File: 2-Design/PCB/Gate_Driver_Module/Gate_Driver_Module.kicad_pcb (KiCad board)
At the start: 2 copper layers, 30 x 30 mm, 12 parts, among them J1 Conn_01x04_Male, J2 Conn_01x04_Male, U1 ROE-0512S, U2 LTV-817, U3 TC4421A

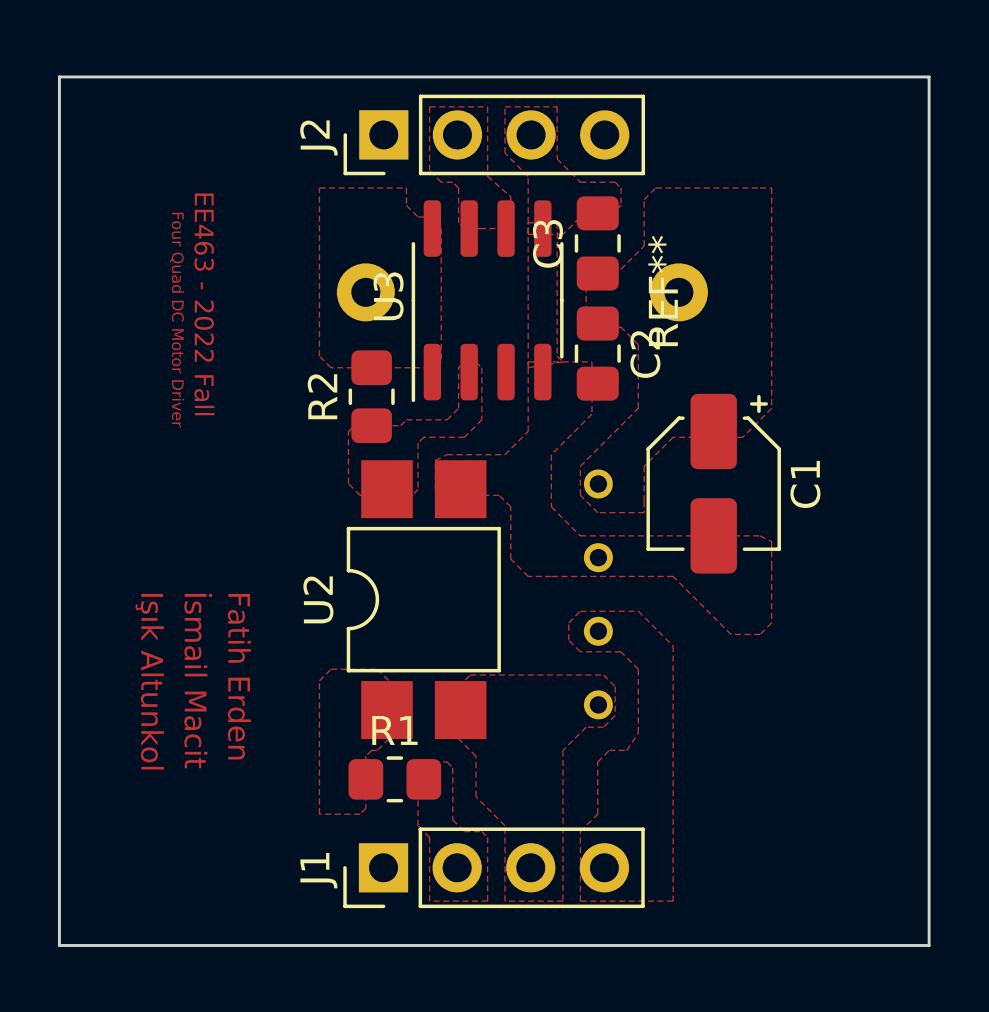
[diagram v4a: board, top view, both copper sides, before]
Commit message: Controller Module v1, tracks to be drawn
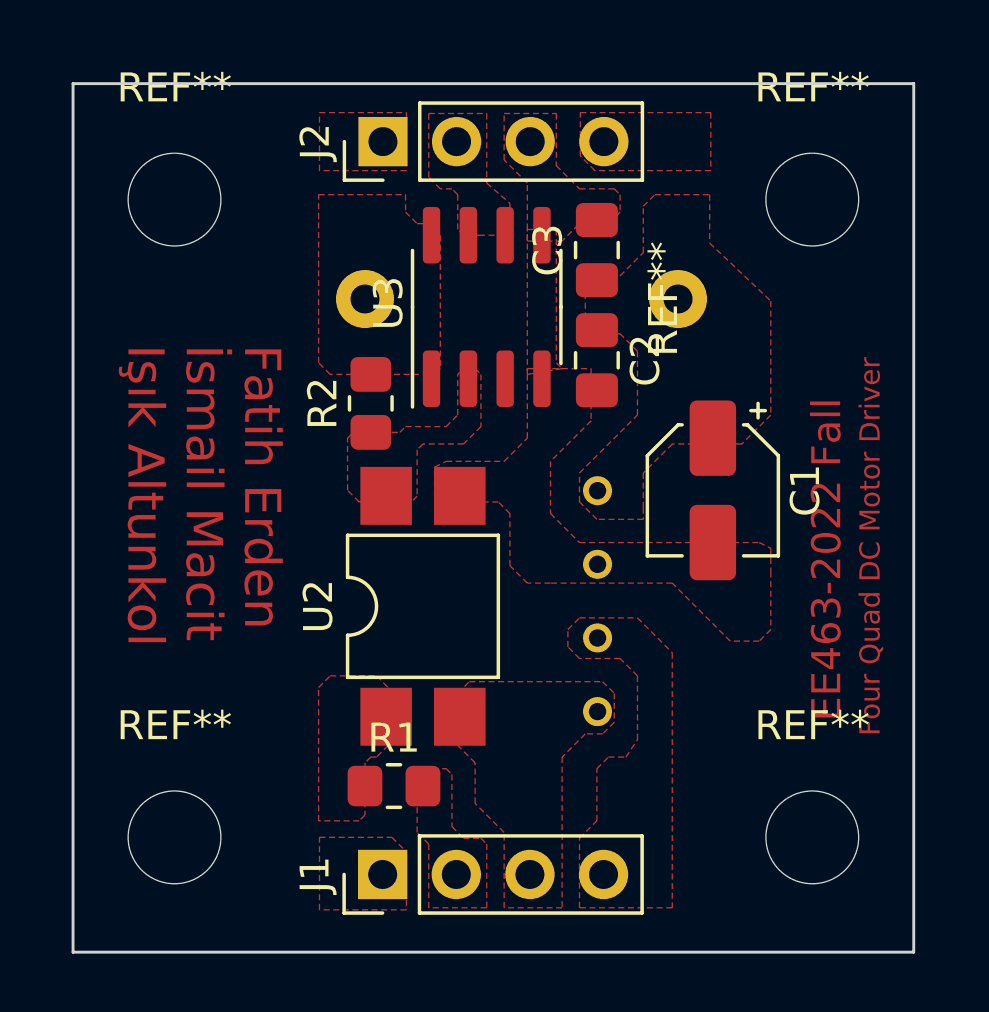
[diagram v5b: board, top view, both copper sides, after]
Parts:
- added REF**: MountingHole_3.2mm_M3_ISO7380, MountingHole:MountingHole_3.2mm_M3_ISO7380, F.Cu at (170.0, 117.0)
- added REF**: MountingHole_3.2mm_M3_ISO7380, MountingHole:MountingHole_3.2mm_M3_ISO7380, F.Cu at (192.0, 117.0)
- added REF**: MountingHole_3.2mm_M3_ISO7380, MountingHole:MountingHole_3.2mm_M3_ISO7380, F.Cu at (192.0, 95.0)
- added REF**: MountingHole_3.2mm_M3_ISO7380, MountingHole:MountingHole_3.2mm_M3_ISO7380, F.Cu at (170.0, 95.0)
- moved ? 0.23 mm to (176.6, 98.4)
- moved C1 0.23 mm to (188.6, 105.0)
- moved C2 0.23 mm to (184.6, 100.5)
- moved C3 0.23 mm to (184.6, 96.7)
- moved J1 0.23 mm to (177.2, 118.3)
- moved J2 0.23 mm to (177.2, 93.0)
- moved R1 0.23 mm to (177.6, 115.2)
- moved R2 0.23 mm to (176.8, 102.0)
- moved REF** 0.23 mm to (187.4, 98.4)
- moved U1 0.23 mm to (184.6, 108.9)
- moved U2 0.23 mm to (178.6, 109.0)
- moved U3 0.23 mm to (180.8, 98.7)
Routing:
- added copper zone on F.Cu, net unconnected-(J1-Pad1)
- added copper zone on F.Cu, net unconnected-(J2-Pad1)
- added copper zone on F.Cu, net unconnected-(J2-Pad4)
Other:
- board size 30 x 30 mm -> 29 x 30 mm
- board text added: "EE463-2022 Fall"
- board text added: "Fatih Erden İsmail Macit Işık Altunkol"
- board text removed: "EE463 - 2022 Fall"
- board text removed: "Fatih Erden"
- board text removed: "Işık Altunkol"
- board text removed: "İsmail Macit"

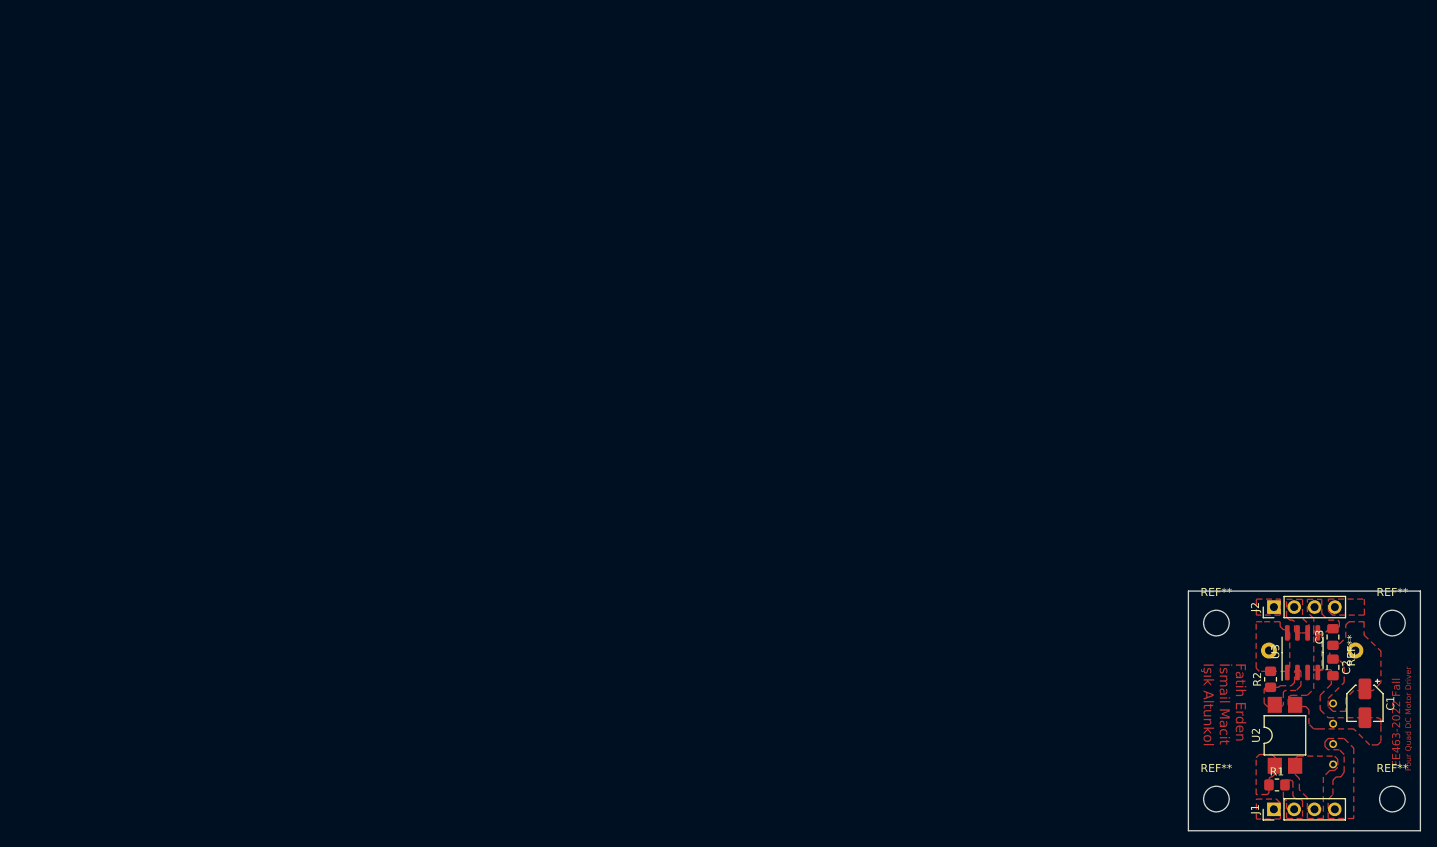
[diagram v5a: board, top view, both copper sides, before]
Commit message: Gate Driver Module minimum load for boost, plus Controller Module advancements
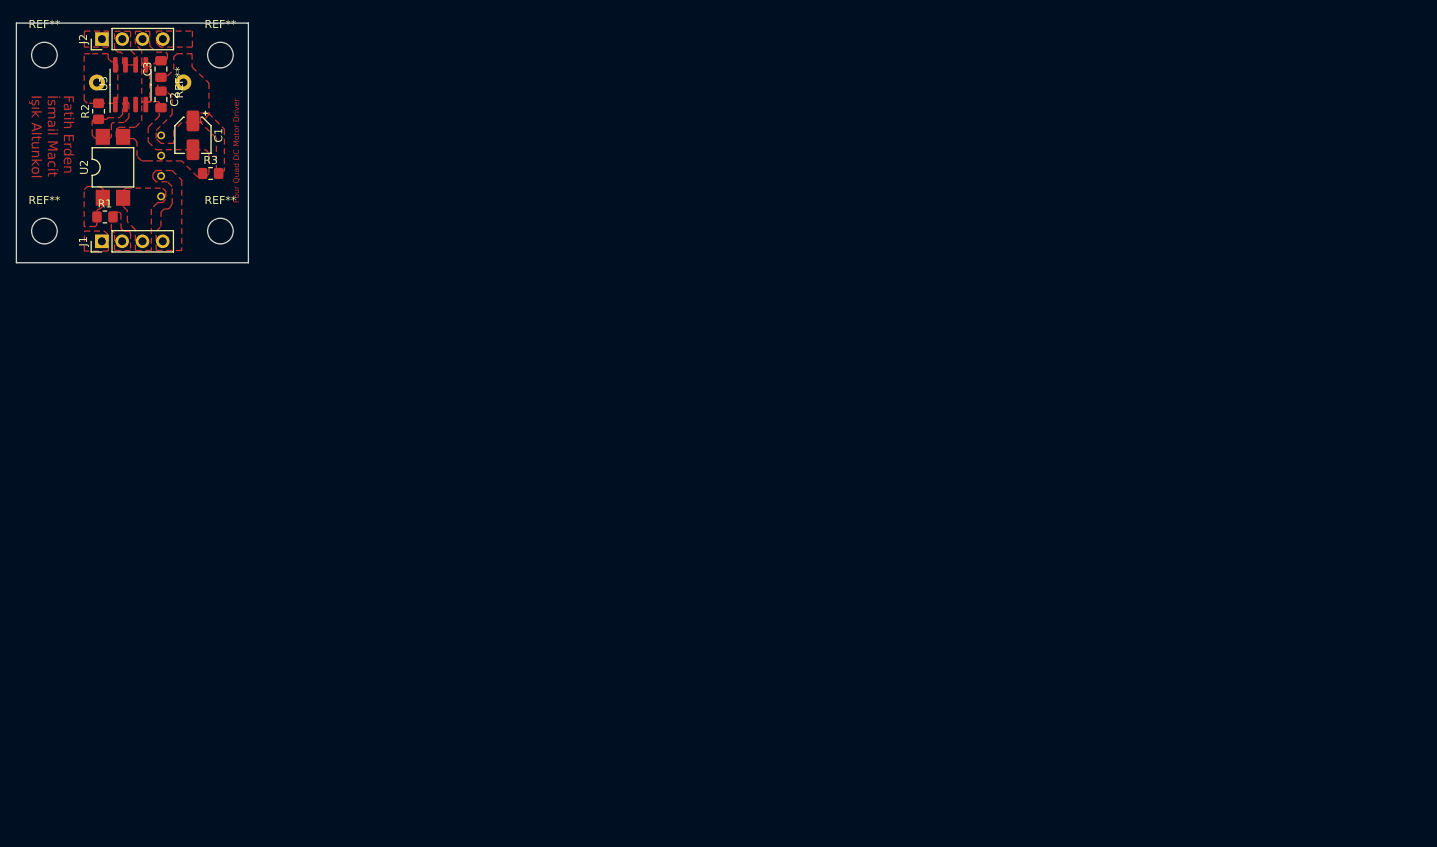
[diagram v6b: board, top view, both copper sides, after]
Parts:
- added R3: 1kR, Resistor_SMD:R_0805_2012Metric_Pad1.20x1.40mm_HandSolder, F.Cu at (44.3, 38.8)
- moved ? 162.8 mm to (30.1, 27.4)
- moved C1 162.8 mm to (42.1, 34.0)
- moved C2 162.8 mm to (38.1, 29.5)
- moved C3 162.8 mm to (38.1, 25.7)
- moved J1 162.8 mm to (30.7, 47.3)
- moved J2 162.8 mm to (30.7, 22.0)
- moved R1 162.8 mm to (31.1, 44.2)
- moved R2 162.8 mm to (30.3, 31.0)
- moved REF** 162.8 mm to (23.5, 46.0)
- moved REF** 162.8 mm to (45.5, 46.0)
- moved REF** 162.8 mm to (45.5, 24.0)
- moved REF** 162.8 mm to (23.5, 24.0)
- moved REF** 162.8 mm to (40.9, 27.4)
- moved U1 162.8 mm to (38.1, 37.9)
- moved U2 162.8 mm to (32.1, 38.0)
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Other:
- board text removed: "EE463-2022 Fall"

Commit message: Some changes i dont even remember
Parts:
- removed the ? at (30.1, 27.4)
- removed the C1 at (42.1, 34.0)
- removed the C2 at (38.1, 29.5)
- removed the C3 at (38.1, 25.7)
- removed the J1 at (30.7, 47.3)
- removed the J2 at (30.7, 22.0)
- removed the R1 at (31.1, 44.2)
- removed the R2 at (30.3, 31.0)
- removed the R3 at (44.3, 38.8)
- removed the REF** at (23.5, 46.0)
- removed the REF** at (45.5, 46.0)
- removed the REF** at (45.5, 24.0)
- removed the REF** at (23.5, 24.0)
- removed the REF** at (40.9, 27.4)
- removed the U1 at (38.1, 37.9)
- removed the U2 at (32.1, 38.0)
- removed the U3 at (34.3, 27.7)
- added ?: , , F.Cu at (71.6, 26.4)
- added ?: , , F.Cu at (246.6, 94.0)
- added ?: , , F.Cu at (211.6, 26.4)
- added ?: , , F.Cu at (176.6, 60.2)
- added ?: , , F.Cu at (141.6, 26.4)
- added ?: , , F.Cu at (106.6, 94.0)
- added ?: , , F.Cu at (176.6, 127.8)
- added ?: , , F.Cu at (211.6, 60.2)
- added ?: , , F.Cu at (246.6, 26.4)
- added ?: , , F.Cu at (176.6, 94.0)
- added ?: , , F.Cu at (211.6, 94.0)
- added ?: , , F.Cu at (176.6, 26.4)
- added ?: , , F.Cu at (141.6, 127.8)
- added ?: , , F.Cu at (106.6, 127.8)
- added ?: , , F.Cu at (71.6, 94.0)
- added ?: , , F.Cu at (106.6, 26.4)
- added ?: , , F.Cu at (141.6, 60.2)
- added ?: , , F.Cu at (106.6, 60.2)
- added ?: , , F.Cu at (141.6, 94.0)
- added ?: , , F.Cu at (71.6, 127.8)
- added ?: , , F.Cu at (246.6, 127.8)
- added ?: , , F.Cu at (71.6, 60.2)
- added ?: , , F.Cu at (246.6, 60.2)
- added ?: , , F.Cu at (211.6, 127.8)
- added C1: 4.7uF, Capacitor_SMD:CP_Elec_4x5.4, F.Cu at (188.6, 134.4)
- added C1: 4.7uF, Capacitor_SMD:CP_Elec_4x5.4, F.Cu at (153.6, 66.8)
- added C1: 4.7uF, Capacitor_SMD:CP_Elec_4x5.4, F.Cu at (83.6, 66.8)
- added C1: 4.7uF, Capacitor_SMD:CP_Elec_4x5.4, F.Cu at (118.6, 100.6)
- added C1: 4.7uF, Capacitor_SMD:CP_Elec_4x5.4, F.Cu at (118.6, 33.0)
- added C1: 4.7uF, Capacitor_SMD:CP_Elec_4x5.4, F.Cu at (188.6, 66.8)
- added C1: 4.7uF, Capacitor_SMD:CP_Elec_4x5.4, F.Cu at (118.6, 66.8)
- added C1: 4.7uF, Capacitor_SMD:CP_Elec_4x5.4, F.Cu at (83.6, 134.4)
- added C1: 4.7uF, Capacitor_SMD:CP_Elec_4x5.4, F.Cu at (153.6, 33.0)
- added C1: 4.7uF, Capacitor_SMD:CP_Elec_4x5.4, F.Cu at (258.6, 66.8)
- added C1: 4.7uF, Capacitor_SMD:CP_Elec_4x5.4, F.Cu at (153.6, 134.4)
- added C1: 4.7uF, Capacitor_SMD:CP_Elec_4x5.4, F.Cu at (153.6, 100.6)
- added C1: 4.7uF, Capacitor_SMD:CP_Elec_4x5.4, F.Cu at (223.6, 100.6)
- added C1: 4.7uF, Capacitor_SMD:CP_Elec_4x5.4, F.Cu at (83.6, 33.0)
- added C1: 4.7uF, Capacitor_SMD:CP_Elec_4x5.4, F.Cu at (258.6, 33.0)
- added C1: 4.7uF, Capacitor_SMD:CP_Elec_4x5.4, F.Cu at (188.6, 33.0)
- added C1: 4.7uF, Capacitor_SMD:CP_Elec_4x5.4, F.Cu at (188.6, 100.6)
- added C1: 4.7uF, Capacitor_SMD:CP_Elec_4x5.4, F.Cu at (223.6, 66.8)
- added C1: 4.7uF, Capacitor_SMD:CP_Elec_4x5.4, F.Cu at (83.6, 100.6)
- added C1: 4.7uF, Capacitor_SMD:CP_Elec_4x5.4, F.Cu at (223.6, 134.4)
- added C1: 4.7uF, Capacitor_SMD:CP_Elec_4x5.4, F.Cu at (258.6, 134.4)
- added C1: 4.7uF, Capacitor_SMD:CP_Elec_4x5.4, F.Cu at (223.6, 33.0)
- added C1: 4.7uF, Capacitor_SMD:CP_Elec_4x5.4, F.Cu at (118.6, 134.4)
- added C1: 4.7uF, Capacitor_SMD:CP_Elec_4x5.4, F.Cu at (258.6, 100.6)
- added C2: 0.1uF, Capacitor_SMD:C_0805_2012Metric_Pad1.18x1.45mm_HandSolder, F.Cu at (149.6, 62.3)
- added C2: 0.1uF, Capacitor_SMD:C_0805_2012Metric_Pad1.18x1.45mm_HandSolder, F.Cu at (114.6, 129.9)
- added C2: 0.1uF, Capacitor_SMD:C_0805_2012Metric_Pad1.18x1.45mm_HandSolder, F.Cu at (219.6, 96.1)
- added C2: 0.1uF, Capacitor_SMD:C_0805_2012Metric_Pad1.18x1.45mm_HandSolder, F.Cu at (149.6, 28.5)
- added C2: 0.1uF, Capacitor_SMD:C_0805_2012Metric_Pad1.18x1.45mm_HandSolder, F.Cu at (79.6, 62.3)
- added C2: 0.1uF, Capacitor_SMD:C_0805_2012Metric_Pad1.18x1.45mm_HandSolder, F.Cu at (79.6, 28.5)
- added C2: 0.1uF, Capacitor_SMD:C_0805_2012Metric_Pad1.18x1.45mm_HandSolder, F.Cu at (254.6, 28.5)
- added C2: 0.1uF, Capacitor_SMD:C_0805_2012Metric_Pad1.18x1.45mm_HandSolder, F.Cu at (184.6, 96.1)
- added C2: 0.1uF, Capacitor_SMD:C_0805_2012Metric_Pad1.18x1.45mm_HandSolder, F.Cu at (184.6, 62.3)
- added C2: 0.1uF, Capacitor_SMD:C_0805_2012Metric_Pad1.18x1.45mm_HandSolder, F.Cu at (184.6, 28.5)
- added C2: 0.1uF, Capacitor_SMD:C_0805_2012Metric_Pad1.18x1.45mm_HandSolder, F.Cu at (114.6, 62.3)
- added C2: 0.1uF, Capacitor_SMD:C_0805_2012Metric_Pad1.18x1.45mm_HandSolder, F.Cu at (114.6, 28.5)
- added C2: 0.1uF, Capacitor_SMD:C_0805_2012Metric_Pad1.18x1.45mm_HandSolder, F.Cu at (79.6, 96.1)
- added C2: 0.1uF, Capacitor_SMD:C_0805_2012Metric_Pad1.18x1.45mm_HandSolder, F.Cu at (149.6, 129.9)
- added C2: 0.1uF, Capacitor_SMD:C_0805_2012Metric_Pad1.18x1.45mm_HandSolder, F.Cu at (219.6, 129.9)
- added C2: 0.1uF, Capacitor_SMD:C_0805_2012Metric_Pad1.18x1.45mm_HandSolder, F.Cu at (184.6, 129.9)
- added C2: 0.1uF, Capacitor_SMD:C_0805_2012Metric_Pad1.18x1.45mm_HandSolder, F.Cu at (219.6, 62.3)
- added C2: 0.1uF, Capacitor_SMD:C_0805_2012Metric_Pad1.18x1.45mm_HandSolder, F.Cu at (219.6, 28.5)
- added C2: 0.1uF, Capacitor_SMD:C_0805_2012Metric_Pad1.18x1.45mm_HandSolder, F.Cu at (254.6, 129.9)
- added C2: 0.1uF, Capacitor_SMD:C_0805_2012Metric_Pad1.18x1.45mm_HandSolder, F.Cu at (114.6, 96.1)
- added C2: 0.1uF, Capacitor_SMD:C_0805_2012Metric_Pad1.18x1.45mm_HandSolder, F.Cu at (254.6, 96.1)
- added C2: 0.1uF, Capacitor_SMD:C_0805_2012Metric_Pad1.18x1.45mm_HandSolder, F.Cu at (79.6, 129.9)
- added C2: 0.1uF, Capacitor_SMD:C_0805_2012Metric_Pad1.18x1.45mm_HandSolder, F.Cu at (254.6, 62.3)
- added C2: 0.1uF, Capacitor_SMD:C_0805_2012Metric_Pad1.18x1.45mm_HandSolder, F.Cu at (149.6, 96.1)
- added C3: 0.1uF, Capacitor_SMD:C_0805_2012Metric_Pad1.18x1.45mm_HandSolder, F.Cu at (114.6, 58.5)
- added C3: 0.1uF, Capacitor_SMD:C_0805_2012Metric_Pad1.18x1.45mm_HandSolder, F.Cu at (184.6, 58.5)
- added C3: 0.1uF, Capacitor_SMD:C_0805_2012Metric_Pad1.18x1.45mm_HandSolder, F.Cu at (79.6, 24.7)
- added C3: 0.1uF, Capacitor_SMD:C_0805_2012Metric_Pad1.18x1.45mm_HandSolder, F.Cu at (114.6, 24.7)
- added C3: 0.1uF, Capacitor_SMD:C_0805_2012Metric_Pad1.18x1.45mm_HandSolder, F.Cu at (219.6, 58.5)
- added C3: 0.1uF, Capacitor_SMD:C_0805_2012Metric_Pad1.18x1.45mm_HandSolder, F.Cu at (219.6, 24.7)
- added C3: 0.1uF, Capacitor_SMD:C_0805_2012Metric_Pad1.18x1.45mm_HandSolder, F.Cu at (149.6, 92.3)
- added C3: 0.1uF, Capacitor_SMD:C_0805_2012Metric_Pad1.18x1.45mm_HandSolder, F.Cu at (79.6, 92.3)
- added C3: 0.1uF, Capacitor_SMD:C_0805_2012Metric_Pad1.18x1.45mm_HandSolder, F.Cu at (219.6, 92.3)
- added C3: 0.1uF, Capacitor_SMD:C_0805_2012Metric_Pad1.18x1.45mm_HandSolder, F.Cu at (184.6, 126.1)
- added C3: 0.1uF, Capacitor_SMD:C_0805_2012Metric_Pad1.18x1.45mm_HandSolder, F.Cu at (184.6, 92.3)
- added C3: 0.1uF, Capacitor_SMD:C_0805_2012Metric_Pad1.18x1.45mm_HandSolder, F.Cu at (149.6, 24.7)
- added C3: 0.1uF, Capacitor_SMD:C_0805_2012Metric_Pad1.18x1.45mm_HandSolder, F.Cu at (254.6, 126.1)
- added C3: 0.1uF, Capacitor_SMD:C_0805_2012Metric_Pad1.18x1.45mm_HandSolder, F.Cu at (149.6, 126.1)
- added C3: 0.1uF, Capacitor_SMD:C_0805_2012Metric_Pad1.18x1.45mm_HandSolder, F.Cu at (254.6, 58.5)
- added C3: 0.1uF, Capacitor_SMD:C_0805_2012Metric_Pad1.18x1.45mm_HandSolder, F.Cu at (254.6, 92.3)
- added C3: 0.1uF, Capacitor_SMD:C_0805_2012Metric_Pad1.18x1.45mm_HandSolder, F.Cu at (184.6, 24.7)
- added C3: 0.1uF, Capacitor_SMD:C_0805_2012Metric_Pad1.18x1.45mm_HandSolder, F.Cu at (149.6, 58.5)
- added C3: 0.1uF, Capacitor_SMD:C_0805_2012Metric_Pad1.18x1.45mm_HandSolder, F.Cu at (79.6, 58.5)
- added C3: 0.1uF, Capacitor_SMD:C_0805_2012Metric_Pad1.18x1.45mm_HandSolder, F.Cu at (114.6, 126.1)
- added C3: 0.1uF, Capacitor_SMD:C_0805_2012Metric_Pad1.18x1.45mm_HandSolder, F.Cu at (254.6, 24.7)
- added C3: 0.1uF, Capacitor_SMD:C_0805_2012Metric_Pad1.18x1.45mm_HandSolder, F.Cu at (114.6, 92.3)
- added C3: 0.1uF, Capacitor_SMD:C_0805_2012Metric_Pad1.18x1.45mm_HandSolder, F.Cu at (79.6, 126.1)
- added C3: 0.1uF, Capacitor_SMD:C_0805_2012Metric_Pad1.18x1.45mm_HandSolder, F.Cu at (219.6, 126.1)
- added J1: Conn_01x04_Male, Connector_PinHeader_2.54mm:PinHeader_1x04_P2.54mm_Vertical, F.Cu at (247.2, 46.3)
- added J1: Conn_01x04_Male, Connector_PinHeader_2.54mm:PinHeader_1x04_P2.54mm_Vertical, F.Cu at (177.2, 80.1)
- added J1: Conn_01x04_Male, Connector_PinHeader_2.54mm:PinHeader_1x04_P2.54mm_Vertical, F.Cu at (247.2, 80.1)
- added J1: Conn_01x04_Male, Connector_PinHeader_2.54mm:PinHeader_1x04_P2.54mm_Vertical, F.Cu at (247.2, 113.9)
- added J1: Conn_01x04_Male, Connector_PinHeader_2.54mm:PinHeader_1x04_P2.54mm_Vertical, F.Cu at (212.2, 113.9)
- added J1: Conn_01x04_Male, Connector_PinHeader_2.54mm:PinHeader_1x04_P2.54mm_Vertical, F.Cu at (72.2, 80.1)
- added J1: Conn_01x04_Male, Connector_PinHeader_2.54mm:PinHeader_1x04_P2.54mm_Vertical, F.Cu at (107.2, 80.1)
- added J1: Conn_01x04_Male, Connector_PinHeader_2.54mm:PinHeader_1x04_P2.54mm_Vertical, F.Cu at (177.2, 113.9)
- added J1: Conn_01x04_Male, Connector_PinHeader_2.54mm:PinHeader_1x04_P2.54mm_Vertical, F.Cu at (107.2, 147.7)
- added J1: Conn_01x04_Male, Connector_PinHeader_2.54mm:PinHeader_1x04_P2.54mm_Vertical, F.Cu at (247.2, 147.7)
- added J1: Conn_01x04_Male, Connector_PinHeader_2.54mm:PinHeader_1x04_P2.54mm_Vertical, F.Cu at (212.2, 147.7)
- added J1: Conn_01x04_Male, Connector_PinHeader_2.54mm:PinHeader_1x04_P2.54mm_Vertical, F.Cu at (212.2, 46.3)
- added J1: Conn_01x04_Male, Connector_PinHeader_2.54mm:PinHeader_1x04_P2.54mm_Vertical, F.Cu at (177.2, 147.7)
- added J1: Conn_01x04_Male, Connector_PinHeader_2.54mm:PinHeader_1x04_P2.54mm_Vertical, F.Cu at (177.2, 46.3)
- added J1: Conn_01x04_Male, Connector_PinHeader_2.54mm:PinHeader_1x04_P2.54mm_Vertical, F.Cu at (72.2, 113.9)
- added J1: Conn_01x04_Male, Connector_PinHeader_2.54mm:PinHeader_1x04_P2.54mm_Vertical, F.Cu at (107.2, 46.3)
- added J1: Conn_01x04_Male, Connector_PinHeader_2.54mm:PinHeader_1x04_P2.54mm_Vertical, F.Cu at (142.2, 113.9)
- added J1: Conn_01x04_Male, Connector_PinHeader_2.54mm:PinHeader_1x04_P2.54mm_Vertical, F.Cu at (212.2, 80.1)
- added J1: Conn_01x04_Male, Connector_PinHeader_2.54mm:PinHeader_1x04_P2.54mm_Vertical, F.Cu at (142.2, 147.7)
- added J1: Conn_01x04_Male, Connector_PinHeader_2.54mm:PinHeader_1x04_P2.54mm_Vertical, F.Cu at (72.2, 147.7)
- added J1: Conn_01x04_Male, Connector_PinHeader_2.54mm:PinHeader_1x04_P2.54mm_Vertical, F.Cu at (142.2, 80.1)
- added J1: Conn_01x04_Male, Connector_PinHeader_2.54mm:PinHeader_1x04_P2.54mm_Vertical, F.Cu at (72.2, 46.3)
- added J1: Conn_01x04_Male, Connector_PinHeader_2.54mm:PinHeader_1x04_P2.54mm_Vertical, F.Cu at (142.2, 46.3)
- added J1: Conn_01x04_Male, Connector_PinHeader_2.54mm:PinHeader_1x04_P2.54mm_Vertical, F.Cu at (107.2, 113.9)
- added J2: Conn_01x04_Male, Connector_PinHeader_2.54mm:PinHeader_1x04_P2.54mm_Vertical, F.Cu at (247.2, 122.4)
- added J2: Conn_01x04_Male, Connector_PinHeader_2.54mm:PinHeader_1x04_P2.54mm_Vertical, F.Cu at (212.2, 21.0)
- added J2: Conn_01x04_Male, Connector_PinHeader_2.54mm:PinHeader_1x04_P2.54mm_Vertical, F.Cu at (107.2, 88.6)
- added J2: Conn_01x04_Male, Connector_PinHeader_2.54mm:PinHeader_1x04_P2.54mm_Vertical, F.Cu at (142.2, 54.8)
- added J2: Conn_01x04_Male, Connector_PinHeader_2.54mm:PinHeader_1x04_P2.54mm_Vertical, F.Cu at (212.2, 122.4)
- added J2: Conn_01x04_Male, Connector_PinHeader_2.54mm:PinHeader_1x04_P2.54mm_Vertical, F.Cu at (177.2, 122.4)
- added J2: Conn_01x04_Male, Connector_PinHeader_2.54mm:PinHeader_1x04_P2.54mm_Vertical, F.Cu at (142.2, 88.6)
- added J2: Conn_01x04_Male, Connector_PinHeader_2.54mm:PinHeader_1x04_P2.54mm_Vertical, F.Cu at (142.2, 122.4)
- added J2: Conn_01x04_Male, Connector_PinHeader_2.54mm:PinHeader_1x04_P2.54mm_Vertical, F.Cu at (212.2, 54.8)
- added J2: Conn_01x04_Male, Connector_PinHeader_2.54mm:PinHeader_1x04_P2.54mm_Vertical, F.Cu at (212.2, 88.6)
- added J2: Conn_01x04_Male, Connector_PinHeader_2.54mm:PinHeader_1x04_P2.54mm_Vertical, F.Cu at (72.2, 88.6)
- added J2: Conn_01x04_Male, Connector_PinHeader_2.54mm:PinHeader_1x04_P2.54mm_Vertical, F.Cu at (247.2, 21.0)
- added J2: Conn_01x04_Male, Connector_PinHeader_2.54mm:PinHeader_1x04_P2.54mm_Vertical, F.Cu at (72.2, 21.0)
- added J2: Conn_01x04_Male, Connector_PinHeader_2.54mm:PinHeader_1x04_P2.54mm_Vertical, F.Cu at (177.2, 88.6)
- added J2: Conn_01x04_Male, Connector_PinHeader_2.54mm:PinHeader_1x04_P2.54mm_Vertical, F.Cu at (72.2, 54.8)
- added J2: Conn_01x04_Male, Connector_PinHeader_2.54mm:PinHeader_1x04_P2.54mm_Vertical, F.Cu at (177.2, 21.0)
- added J2: Conn_01x04_Male, Connector_PinHeader_2.54mm:PinHeader_1x04_P2.54mm_Vertical, F.Cu at (107.2, 21.0)
- added J2: Conn_01x04_Male, Connector_PinHeader_2.54mm:PinHeader_1x04_P2.54mm_Vertical, F.Cu at (72.2, 122.4)
- added J2: Conn_01x04_Male, Connector_PinHeader_2.54mm:PinHeader_1x04_P2.54mm_Vertical, F.Cu at (142.2, 21.0)
- added J2: Conn_01x04_Male, Connector_PinHeader_2.54mm:PinHeader_1x04_P2.54mm_Vertical, F.Cu at (177.2, 54.8)
- added J2: Conn_01x04_Male, Connector_PinHeader_2.54mm:PinHeader_1x04_P2.54mm_Vertical, F.Cu at (107.2, 122.4)
- added J2: Conn_01x04_Male, Connector_PinHeader_2.54mm:PinHeader_1x04_P2.54mm_Vertical, F.Cu at (107.2, 54.8)
- added J2: Conn_01x04_Male, Connector_PinHeader_2.54mm:PinHeader_1x04_P2.54mm_Vertical, F.Cu at (247.2, 88.6)
- added J2: Conn_01x04_Male, Connector_PinHeader_2.54mm:PinHeader_1x04_P2.54mm_Vertical, F.Cu at (247.2, 54.8)
- added R1: 330R, Resistor_SMD:R_0805_2012Metric_Pad1.20x1.40mm_HandSolder, F.Cu at (72.6, 43.2)
- added R1: 330R, Resistor_SMD:R_0805_2012Metric_Pad1.20x1.40mm_HandSolder, F.Cu at (177.6, 43.2)
- added R1: 330R, Resistor_SMD:R_0805_2012Metric_Pad1.20x1.40mm_HandSolder, F.Cu at (212.6, 43.2)
- added R1: 330R, Resistor_SMD:R_0805_2012Metric_Pad1.20x1.40mm_HandSolder, F.Cu at (72.6, 110.8)
- added R1: 330R, Resistor_SMD:R_0805_2012Metric_Pad1.20x1.40mm_HandSolder, F.Cu at (212.6, 110.8)
- added R1: 330R, Resistor_SMD:R_0805_2012Metric_Pad1.20x1.40mm_HandSolder, F.Cu at (247.6, 110.8)
- added R1: 330R, Resistor_SMD:R_0805_2012Metric_Pad1.20x1.40mm_HandSolder, F.Cu at (177.6, 77.0)
- added R1: 330R, Resistor_SMD:R_0805_2012Metric_Pad1.20x1.40mm_HandSolder, F.Cu at (107.6, 77.0)
- added R1: 330R, Resistor_SMD:R_0805_2012Metric_Pad1.20x1.40mm_HandSolder, F.Cu at (142.6, 144.6)
- added R1: 330R, Resistor_SMD:R_0805_2012Metric_Pad1.20x1.40mm_HandSolder, F.Cu at (107.6, 110.8)
- added R1: 330R, Resistor_SMD:R_0805_2012Metric_Pad1.20x1.40mm_HandSolder, F.Cu at (107.6, 144.6)
- added R1: 330R, Resistor_SMD:R_0805_2012Metric_Pad1.20x1.40mm_HandSolder, F.Cu at (212.6, 144.6)
- added R1: 330R, Resistor_SMD:R_0805_2012Metric_Pad1.20x1.40mm_HandSolder, F.Cu at (107.6, 43.2)
- added R1: 330R, Resistor_SMD:R_0805_2012Metric_Pad1.20x1.40mm_HandSolder, F.Cu at (212.6, 77.0)
- added R1: 330R, Resistor_SMD:R_0805_2012Metric_Pad1.20x1.40mm_HandSolder, F.Cu at (177.6, 144.6)
- added R1: 330R, Resistor_SMD:R_0805_2012Metric_Pad1.20x1.40mm_HandSolder, F.Cu at (247.6, 144.6)
- added R1: 330R, Resistor_SMD:R_0805_2012Metric_Pad1.20x1.40mm_HandSolder, F.Cu at (72.6, 77.0)
- added R1: 330R, Resistor_SMD:R_0805_2012Metric_Pad1.20x1.40mm_HandSolder, F.Cu at (247.6, 43.2)
- added R1: 330R, Resistor_SMD:R_0805_2012Metric_Pad1.20x1.40mm_HandSolder, F.Cu at (142.6, 110.8)
- added R1: 330R, Resistor_SMD:R_0805_2012Metric_Pad1.20x1.40mm_HandSolder, F.Cu at (142.6, 43.2)
- added R1: 330R, Resistor_SMD:R_0805_2012Metric_Pad1.20x1.40mm_HandSolder, F.Cu at (247.6, 77.0)
- added R1: 330R, Resistor_SMD:R_0805_2012Metric_Pad1.20x1.40mm_HandSolder, F.Cu at (142.6, 77.0)
- added R1: 330R, Resistor_SMD:R_0805_2012Metric_Pad1.20x1.40mm_HandSolder, F.Cu at (72.6, 144.6)
- added R1: 330R, Resistor_SMD:R_0805_2012Metric_Pad1.20x1.40mm_HandSolder, F.Cu at (177.6, 110.8)
- added R2: 470R, Resistor_SMD:R_0805_2012Metric_Pad1.20x1.40mm_HandSolder, F.Cu at (106.8, 30.0)
- added R2: 470R, Resistor_SMD:R_0805_2012Metric_Pad1.20x1.40mm_HandSolder, F.Cu at (246.8, 97.6)
- added R2: 470R, Resistor_SMD:R_0805_2012Metric_Pad1.20x1.40mm_HandSolder, F.Cu at (141.8, 30.0)
- added R2: 470R, Resistor_SMD:R_0805_2012Metric_Pad1.20x1.40mm_HandSolder, F.Cu at (71.8, 97.6)
- added R2: 470R, Resistor_SMD:R_0805_2012Metric_Pad1.20x1.40mm_HandSolder, F.Cu at (246.8, 131.4)
- added R2: 470R, Resistor_SMD:R_0805_2012Metric_Pad1.20x1.40mm_HandSolder, F.Cu at (176.8, 63.8)
- added R2: 470R, Resistor_SMD:R_0805_2012Metric_Pad1.20x1.40mm_HandSolder, F.Cu at (71.8, 131.4)
- added R2: 470R, Resistor_SMD:R_0805_2012Metric_Pad1.20x1.40mm_HandSolder, F.Cu at (211.8, 63.8)
- added R2: 470R, Resistor_SMD:R_0805_2012Metric_Pad1.20x1.40mm_HandSolder, F.Cu at (176.8, 131.4)
- added R2: 470R, Resistor_SMD:R_0805_2012Metric_Pad1.20x1.40mm_HandSolder, F.Cu at (106.8, 97.6)
- added R2: 470R, Resistor_SMD:R_0805_2012Metric_Pad1.20x1.40mm_HandSolder, F.Cu at (141.8, 63.8)
- added R2: 470R, Resistor_SMD:R_0805_2012Metric_Pad1.20x1.40mm_HandSolder, F.Cu at (246.8, 30.0)
- added R2: 470R, Resistor_SMD:R_0805_2012Metric_Pad1.20x1.40mm_HandSolder, F.Cu at (211.8, 97.6)
- added R2: 470R, Resistor_SMD:R_0805_2012Metric_Pad1.20x1.40mm_HandSolder, F.Cu at (141.8, 97.6)
- added R2: 470R, Resistor_SMD:R_0805_2012Metric_Pad1.20x1.40mm_HandSolder, F.Cu at (71.8, 63.8)
- added R2: 470R, Resistor_SMD:R_0805_2012Metric_Pad1.20x1.40mm_HandSolder, F.Cu at (141.8, 131.4)
- added R2: 470R, Resistor_SMD:R_0805_2012Metric_Pad1.20x1.40mm_HandSolder, F.Cu at (176.8, 97.6)
- added R2: 470R, Resistor_SMD:R_0805_2012Metric_Pad1.20x1.40mm_HandSolder, F.Cu at (211.8, 131.4)
- added R2: 470R, Resistor_SMD:R_0805_2012Metric_Pad1.20x1.40mm_HandSolder, F.Cu at (176.8, 30.0)
- added R2: 470R, Resistor_SMD:R_0805_2012Metric_Pad1.20x1.40mm_HandSolder, F.Cu at (211.8, 30.0)
- added R2: 470R, Resistor_SMD:R_0805_2012Metric_Pad1.20x1.40mm_HandSolder, F.Cu at (106.8, 131.4)
- added R2: 470R, Resistor_SMD:R_0805_2012Metric_Pad1.20x1.40mm_HandSolder, F.Cu at (71.8, 30.0)
- added R2: 470R, Resistor_SMD:R_0805_2012Metric_Pad1.20x1.40mm_HandSolder, F.Cu at (246.8, 63.8)
- added R2: 470R, Resistor_SMD:R_0805_2012Metric_Pad1.20x1.40mm_HandSolder, F.Cu at (106.8, 63.8)
- added R3: 1kR, Resistor_SMD:R_0805_2012Metric_Pad1.20x1.40mm_HandSolder, F.Cu at (85.8, 105.4)
- added R3: 1kR, Resistor_SMD:R_0805_2012Metric_Pad1.20x1.40mm_HandSolder, F.Cu at (225.8, 105.4)
- added R3: 1kR, Resistor_SMD:R_0805_2012Metric_Pad1.20x1.40mm_HandSolder, F.Cu at (155.8, 105.4)
- added R3: 1kR, Resistor_SMD:R_0805_2012Metric_Pad1.20x1.40mm_HandSolder, F.Cu at (260.8, 37.8)
- added R3: 1kR, Resistor_SMD:R_0805_2012Metric_Pad1.20x1.40mm_HandSolder, F.Cu at (85.8, 37.8)
- added R3: 1kR, Resistor_SMD:R_0805_2012Metric_Pad1.20x1.40mm_HandSolder, F.Cu at (190.8, 37.8)
- added R3: 1kR, Resistor_SMD:R_0805_2012Metric_Pad1.20x1.40mm_HandSolder, F.Cu at (190.8, 71.6)
- added R3: 1kR, Resistor_SMD:R_0805_2012Metric_Pad1.20x1.40mm_HandSolder, F.Cu at (190.8, 105.4)
- added R3: 1kR, Resistor_SMD:R_0805_2012Metric_Pad1.20x1.40mm_HandSolder, F.Cu at (190.8, 139.2)
- added R3: 1kR, Resistor_SMD:R_0805_2012Metric_Pad1.20x1.40mm_HandSolder, F.Cu at (225.8, 71.6)
- added R3: 1kR, Resistor_SMD:R_0805_2012Metric_Pad1.20x1.40mm_HandSolder, F.Cu at (85.8, 139.2)
- added R3: 1kR, Resistor_SMD:R_0805_2012Metric_Pad1.20x1.40mm_HandSolder, F.Cu at (155.8, 37.8)
- added R3: 1kR, Resistor_SMD:R_0805_2012Metric_Pad1.20x1.40mm_HandSolder, F.Cu at (260.8, 105.4)
- added R3: 1kR, Resistor_SMD:R_0805_2012Metric_Pad1.20x1.40mm_HandSolder, F.Cu at (120.8, 71.6)
- added R3: 1kR, Resistor_SMD:R_0805_2012Metric_Pad1.20x1.40mm_HandSolder, F.Cu at (120.8, 37.8)
- added R3: 1kR, Resistor_SMD:R_0805_2012Metric_Pad1.20x1.40mm_HandSolder, F.Cu at (260.8, 71.6)
- added R3: 1kR, Resistor_SMD:R_0805_2012Metric_Pad1.20x1.40mm_HandSolder, F.Cu at (225.8, 139.2)
- added R3: 1kR, Resistor_SMD:R_0805_2012Metric_Pad1.20x1.40mm_HandSolder, F.Cu at (85.8, 71.6)
- added R3: 1kR, Resistor_SMD:R_0805_2012Metric_Pad1.20x1.40mm_HandSolder, F.Cu at (120.8, 139.2)
- added R3: 1kR, Resistor_SMD:R_0805_2012Metric_Pad1.20x1.40mm_HandSolder, F.Cu at (225.8, 37.8)
- added R3: 1kR, Resistor_SMD:R_0805_2012Metric_Pad1.20x1.40mm_HandSolder, F.Cu at (155.8, 139.2)
- added R3: 1kR, Resistor_SMD:R_0805_2012Metric_Pad1.20x1.40mm_HandSolder, F.Cu at (260.8, 139.2)
- added R3: 1kR, Resistor_SMD:R_0805_2012Metric_Pad1.20x1.40mm_HandSolder, F.Cu at (155.8, 71.6)
- added R3: 1kR, Resistor_SMD:R_0805_2012Metric_Pad1.20x1.40mm_HandSolder, F.Cu at (120.8, 105.4)
- added REF**: Jumper_Wire_Hole, ee463_footprint_lib:Jumper_Wire_Hole, F.Cu at (187.4, 60.2)
- added REF**: MountingHole_3.2mm_M3_ISO7380, MountingHole:MountingHole_3.2mm_M3_ISO7380, F.Cu at (122.0, 124.4)
- added REF**: Jumper_Wire_Hole, ee463_footprint_lib:Jumper_Wire_Hole, F.Cu at (257.4, 60.2)
- added REF**: MountingHole_3.2mm_M3_ISO7380, MountingHole:MountingHole_3.2mm_M3_ISO7380, F.Cu at (135.0, 112.6)
- added REF**: MountingHole_3.2mm_M3_ISO7380, MountingHole:MountingHole_3.2mm_M3_ISO7380, F.Cu at (192.0, 112.6)
- added REF**: MountingHole_3.2mm_M3_ISO7380, MountingHole:MountingHole_3.2mm_M3_ISO7380, F.Cu at (170.0, 124.4)
- added REF**: MountingHole_3.2mm_M3_ISO7380, MountingHole:MountingHole_3.2mm_M3_ISO7380, F.Cu at (240.0, 124.4)
- added REF**: MountingHole_3.2mm_M3_ISO7380, MountingHole:MountingHole_3.2mm_M3_ISO7380, F.Cu at (100.0, 78.8)
- added REF**: MountingHole_3.2mm_M3_ISO7380, MountingHole:MountingHole_3.2mm_M3_ISO7380, F.Cu at (205.0, 124.4)
- added REF**: MountingHole_3.2mm_M3_ISO7380, MountingHole:MountingHole_3.2mm_M3_ISO7380, F.Cu at (192.0, 56.8)
- added REF**: MountingHole_3.2mm_M3_ISO7380, MountingHole:MountingHole_3.2mm_M3_ISO7380, F.Cu at (205.0, 45.0)
- added REF**: MountingHole_3.2mm_M3_ISO7380, MountingHole:MountingHole_3.2mm_M3_ISO7380, F.Cu at (157.0, 23.0)
- added REF**: MountingHole_3.2mm_M3_ISO7380, MountingHole:MountingHole_3.2mm_M3_ISO7380, F.Cu at (170.0, 90.6)
- added REF**: Jumper_Wire_Hole, ee463_footprint_lib:Jumper_Wire_Hole, F.Cu at (117.4, 60.2)
- added REF**: MountingHole_3.2mm_M3_ISO7380, MountingHole:MountingHole_3.2mm_M3_ISO7380, F.Cu at (240.0, 146.4)
- added REF**: Jumper_Wire_Hole, ee463_footprint_lib:Jumper_Wire_Hole, F.Cu at (222.4, 94.0)
- added REF**: Jumper_Wire_Hole, ee463_footprint_lib:Jumper_Wire_Hole, F.Cu at (117.4, 127.8)
- added REF**: MountingHole_3.2mm_M3_ISO7380, MountingHole:MountingHole_3.2mm_M3_ISO7380, F.Cu at (157.0, 45.0)
- added REF**: MountingHole_3.2mm_M3_ISO7380, MountingHole:MountingHole_3.2mm_M3_ISO7380, F.Cu at (87.0, 124.4)
- added REF**: MountingHole_3.2mm_M3_ISO7380, MountingHole:MountingHole_3.2mm_M3_ISO7380, F.Cu at (65.0, 90.6)
- added REF**: MountingHole_3.2mm_M3_ISO7380, MountingHole:MountingHole_3.2mm_M3_ISO7380, F.Cu at (170.0, 112.6)
- added REF**: MountingHole_3.2mm_M3_ISO7380, MountingHole:MountingHole_3.2mm_M3_ISO7380, F.Cu at (240.0, 23.0)
- added REF**: MountingHole_3.2mm_M3_ISO7380, MountingHole:MountingHole_3.2mm_M3_ISO7380, F.Cu at (135.0, 124.4)
- added REF**: MountingHole_3.2mm_M3_ISO7380, MountingHole:MountingHole_3.2mm_M3_ISO7380, F.Cu at (192.0, 146.4)
- added REF**: MountingHole_3.2mm_M3_ISO7380, MountingHole:MountingHole_3.2mm_M3_ISO7380, F.Cu at (170.0, 56.8)
- added REF**: MountingHole_3.2mm_M3_ISO7380, MountingHole:MountingHole_3.2mm_M3_ISO7380, F.Cu at (262.0, 56.8)
- added REF**: MountingHole_3.2mm_M3_ISO7380, MountingHole:MountingHole_3.2mm_M3_ISO7380, F.Cu at (262.0, 45.0)
- added REF**: MountingHole_3.2mm_M3_ISO7380, MountingHole:MountingHole_3.2mm_M3_ISO7380, F.Cu at (157.0, 146.4)
- added REF**: MountingHole_3.2mm_M3_ISO7380, MountingHole:MountingHole_3.2mm_M3_ISO7380, F.Cu at (135.0, 45.0)
- added REF**: MountingHole_3.2mm_M3_ISO7380, MountingHole:MountingHole_3.2mm_M3_ISO7380, F.Cu at (135.0, 56.8)
- added REF**: MountingHole_3.2mm_M3_ISO7380, MountingHole:MountingHole_3.2mm_M3_ISO7380, F.Cu at (240.0, 56.8)
- added REF**: MountingHole_3.2mm_M3_ISO7380, MountingHole:MountingHole_3.2mm_M3_ISO7380, F.Cu at (122.0, 112.6)
- added REF**: MountingHole_3.2mm_M3_ISO7380, MountingHole:MountingHole_3.2mm_M3_ISO7380, F.Cu at (192.0, 45.0)
- added REF**: MountingHole_3.2mm_M3_ISO7380, MountingHole:MountingHole_3.2mm_M3_ISO7380, F.Cu at (205.0, 112.6)
- added REF**: MountingHole_3.2mm_M3_ISO7380, MountingHole:MountingHole_3.2mm_M3_ISO7380, F.Cu at (87.0, 90.6)
- added REF**: MountingHole_3.2mm_M3_ISO7380, MountingHole:MountingHole_3.2mm_M3_ISO7380, F.Cu at (65.0, 56.8)
- added REF**: MountingHole_3.2mm_M3_ISO7380, MountingHole:MountingHole_3.2mm_M3_ISO7380, F.Cu at (87.0, 45.0)
- added REF**: Jumper_Wire_Hole, ee463_footprint_lib:Jumper_Wire_Hole, F.Cu at (187.4, 94.0)
- added REF**: MountingHole_3.2mm_M3_ISO7380, MountingHole:MountingHole_3.2mm_M3_ISO7380, F.Cu at (227.0, 112.6)
- added REF**: MountingHole_3.2mm_M3_ISO7380, MountingHole:MountingHole_3.2mm_M3_ISO7380, F.Cu at (192.0, 78.8)
- added REF**: MountingHole_3.2mm_M3_ISO7380, MountingHole:MountingHole_3.2mm_M3_ISO7380, F.Cu at (192.0, 23.0)
- added REF**: MountingHole_3.2mm_M3_ISO7380, MountingHole:MountingHole_3.2mm_M3_ISO7380, F.Cu at (157.0, 124.4)
- added REF**: MountingHole_3.2mm_M3_ISO7380, MountingHole:MountingHole_3.2mm_M3_ISO7380, F.Cu at (135.0, 78.8)
- added REF**: Jumper_Wire_Hole, ee463_footprint_lib:Jumper_Wire_Hole, F.Cu at (257.4, 26.4)
- added REF**: MountingHole_3.2mm_M3_ISO7380, MountingHole:MountingHole_3.2mm_M3_ISO7380, F.Cu at (240.0, 112.6)
- added REF**: MountingHole_3.2mm_M3_ISO7380, MountingHole:MountingHole_3.2mm_M3_ISO7380, F.Cu at (100.0, 45.0)
- added REF**: MountingHole_3.2mm_M3_ISO7380, MountingHole:MountingHole_3.2mm_M3_ISO7380, F.Cu at (240.0, 45.0)
- added REF**: MountingHole_3.2mm_M3_ISO7380, MountingHole:MountingHole_3.2mm_M3_ISO7380, F.Cu at (170.0, 78.8)
- added REF**: MountingHole_3.2mm_M3_ISO7380, MountingHole:MountingHole_3.2mm_M3_ISO7380, F.Cu at (100.0, 112.6)
- added REF**: MountingHole_3.2mm_M3_ISO7380, MountingHole:MountingHole_3.2mm_M3_ISO7380, F.Cu at (192.0, 124.4)
- added REF**: MountingHole_3.2mm_M3_ISO7380, MountingHole:MountingHole_3.2mm_M3_ISO7380, F.Cu at (205.0, 90.6)
- added REF**: Jumper_Wire_Hole, ee463_footprint_lib:Jumper_Wire_Hole, F.Cu at (257.4, 94.0)
- added REF**: MountingHole_3.2mm_M3_ISO7380, MountingHole:MountingHole_3.2mm_M3_ISO7380, F.Cu at (227.0, 56.8)
- added REF**: Jumper_Wire_Hole, ee463_footprint_lib:Jumper_Wire_Hole, F.Cu at (222.4, 26.4)
- added REF**: MountingHole_3.2mm_M3_ISO7380, MountingHole:MountingHole_3.2mm_M3_ISO7380, F.Cu at (65.0, 146.4)
- added REF**: Jumper_Wire_Hole, ee463_footprint_lib:Jumper_Wire_Hole, F.Cu at (82.4, 60.2)
- added REF**: MountingHole_3.2mm_M3_ISO7380, MountingHole:MountingHole_3.2mm_M3_ISO7380, F.Cu at (87.0, 56.8)
- added REF**: MountingHole_3.2mm_M3_ISO7380, MountingHole:MountingHole_3.2mm_M3_ISO7380, F.Cu at (122.0, 78.8)
- added REF**: MountingHole_3.2mm_M3_ISO7380, MountingHole:MountingHole_3.2mm_M3_ISO7380, F.Cu at (262.0, 23.0)
- added REF**: MountingHole_3.2mm_M3_ISO7380, MountingHole:MountingHole_3.2mm_M3_ISO7380, F.Cu at (262.0, 90.6)
- added REF**: MountingHole_3.2mm_M3_ISO7380, MountingHole:MountingHole_3.2mm_M3_ISO7380, F.Cu at (65.0, 112.6)
- added REF**: MountingHole_3.2mm_M3_ISO7380, MountingHole:MountingHole_3.2mm_M3_ISO7380, F.Cu at (157.0, 90.6)
- added REF**: MountingHole_3.2mm_M3_ISO7380, MountingHole:MountingHole_3.2mm_M3_ISO7380, F.Cu at (65.0, 78.8)
- added REF**: MountingHole_3.2mm_M3_ISO7380, MountingHole:MountingHole_3.2mm_M3_ISO7380, F.Cu at (262.0, 78.8)
- added REF**: Jumper_Wire_Hole, ee463_footprint_lib:Jumper_Wire_Hole, F.Cu at (187.4, 26.4)
- added REF**: MountingHole_3.2mm_M3_ISO7380, MountingHole:MountingHole_3.2mm_M3_ISO7380, F.Cu at (157.0, 78.8)
- added REF**: MountingHole_3.2mm_M3_ISO7380, MountingHole:MountingHole_3.2mm_M3_ISO7380, F.Cu at (262.0, 112.6)
- added REF**: Jumper_Wire_Hole, ee463_footprint_lib:Jumper_Wire_Hole, F.Cu at (257.4, 127.8)
- added REF**: Jumper_Wire_Hole, ee463_footprint_lib:Jumper_Wire_Hole, F.Cu at (187.4, 127.8)
- added REF**: MountingHole_3.2mm_M3_ISO7380, MountingHole:MountingHole_3.2mm_M3_ISO7380, F.Cu at (65.0, 45.0)
- added REF**: MountingHole_3.2mm_M3_ISO7380, MountingHole:MountingHole_3.2mm_M3_ISO7380, F.Cu at (192.0, 90.6)
- added REF**: MountingHole_3.2mm_M3_ISO7380, MountingHole:MountingHole_3.2mm_M3_ISO7380, F.Cu at (205.0, 78.8)
- added REF**: MountingHole_3.2mm_M3_ISO7380, MountingHole:MountingHole_3.2mm_M3_ISO7380, F.Cu at (65.0, 124.4)
- added REF**: MountingHole_3.2mm_M3_ISO7380, MountingHole:MountingHole_3.2mm_M3_ISO7380, F.Cu at (100.0, 146.4)
- added REF**: MountingHole_3.2mm_M3_ISO7380, MountingHole:MountingHole_3.2mm_M3_ISO7380, F.Cu at (157.0, 56.8)
- added REF**: Jumper_Wire_Hole, ee463_footprint_lib:Jumper_Wire_Hole, F.Cu at (222.4, 60.2)
- added REF**: Jumper_Wire_Hole, ee463_footprint_lib:Jumper_Wire_Hole, F.Cu at (152.4, 127.8)
- added REF**: MountingHole_3.2mm_M3_ISO7380, MountingHole:MountingHole_3.2mm_M3_ISO7380, F.Cu at (170.0, 146.4)
- added REF**: MountingHole_3.2mm_M3_ISO7380, MountingHole:MountingHole_3.2mm_M3_ISO7380, F.Cu at (122.0, 90.6)
- added REF**: MountingHole_3.2mm_M3_ISO7380, MountingHole:MountingHole_3.2mm_M3_ISO7380, F.Cu at (87.0, 78.8)
- added REF**: MountingHole_3.2mm_M3_ISO7380, MountingHole:MountingHole_3.2mm_M3_ISO7380, F.Cu at (100.0, 90.6)
- added REF**: Jumper_Wire_Hole, ee463_footprint_lib:Jumper_Wire_Hole, F.Cu at (222.4, 127.8)
- added REF**: MountingHole_3.2mm_M3_ISO7380, MountingHole:MountingHole_3.2mm_M3_ISO7380, F.Cu at (135.0, 23.0)
- added REF**: MountingHole_3.2mm_M3_ISO7380, MountingHole:MountingHole_3.2mm_M3_ISO7380, F.Cu at (87.0, 112.6)
- added REF**: MountingHole_3.2mm_M3_ISO7380, MountingHole:MountingHole_3.2mm_M3_ISO7380, F.Cu at (87.0, 146.4)
- added REF**: MountingHole_3.2mm_M3_ISO7380, MountingHole:MountingHole_3.2mm_M3_ISO7380, F.Cu at (205.0, 146.4)
- added REF**: MountingHole_3.2mm_M3_ISO7380, MountingHole:MountingHole_3.2mm_M3_ISO7380, F.Cu at (135.0, 146.4)
- added REF**: Jumper_Wire_Hole, ee463_footprint_lib:Jumper_Wire_Hole, F.Cu at (117.4, 94.0)
- added REF**: MountingHole_3.2mm_M3_ISO7380, MountingHole:MountingHole_3.2mm_M3_ISO7380, F.Cu at (205.0, 23.0)
- added REF**: Jumper_Wire_Hole, ee463_footprint_lib:Jumper_Wire_Hole, F.Cu at (152.4, 94.0)
- added REF**: Jumper_Wire_Hole, ee463_footprint_lib:Jumper_Wire_Hole, F.Cu at (82.4, 94.0)
- added REF**: MountingHole_3.2mm_M3_ISO7380, MountingHole:MountingHole_3.2mm_M3_ISO7380, F.Cu at (262.0, 146.4)
- added REF**: MountingHole_3.2mm_M3_ISO7380, MountingHole:MountingHole_3.2mm_M3_ISO7380, F.Cu at (170.0, 23.0)
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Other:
- board size 29 x 30 mm -> 207.8 x 135.2 mm
